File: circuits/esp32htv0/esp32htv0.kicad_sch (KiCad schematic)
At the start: 42 parts, among them J1 Power, J2 UART, SW1 EN, SW2 BOOT, U1 LD1117S33TR_SOT223, U2 ESP32-WROOM-32UE, U3 BME280

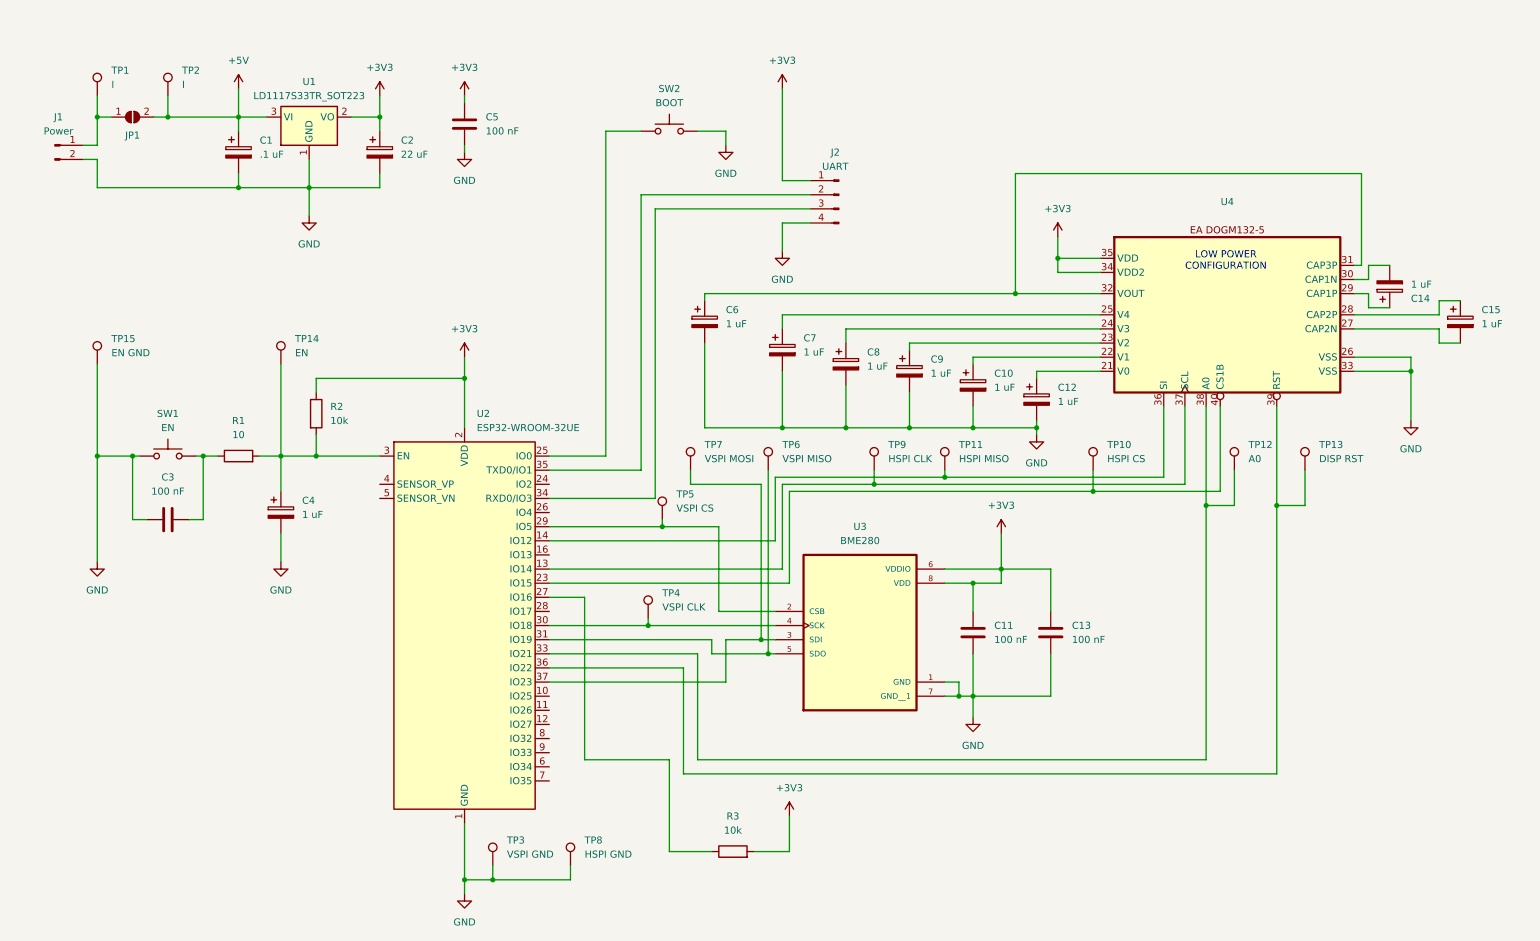
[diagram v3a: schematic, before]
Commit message: Adding data-sheets, documentation and updated circuit for the ESP32 HTV project
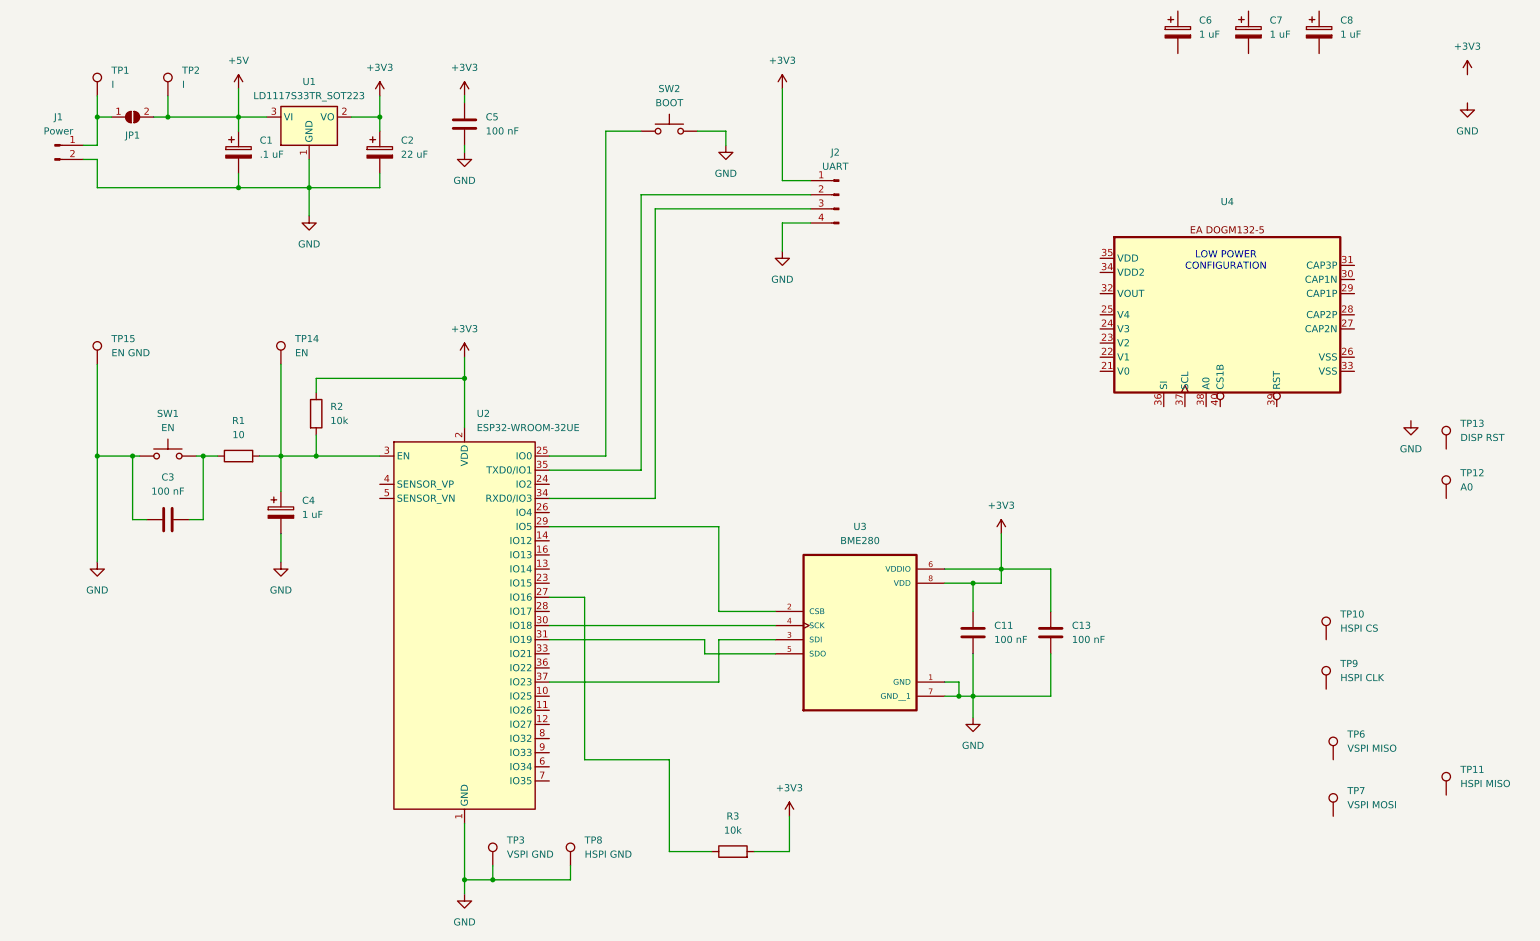
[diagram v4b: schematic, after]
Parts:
- removed C10, C12, C14, C15, C9: 1 uF, Capacitor_SMD:C_1206_3216Metric_Pad1.33x1.80mm_HandSolder, symbol Device:C_Polarized
- removed TP4: VSPI CLK, TestPoint:TestPoint_Loop_D2.50mm_Drill1.0mm, symbol Connector:TestPoint
- removed TP5: VSPI CS, TestPoint:TestPoint_Loop_D2.50mm_Drill1.0mm, symbol Connector:TestPoint
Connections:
- net +3V3: no longer U4.34 (VDD2), U4.35 (VDD)
- net GND: no longer C6.2, C7.2, C8.2, U4.26 (VSS), U4.33 (VSS)
- net at U4.24 (V3): no longer C8.1
- net at U4.25 (V4): no longer C7.1
- net at U2.31 (IO19), U3.5 (SDO): no longer TP6.1
- net at U2.37 (IO23), U3.3 (SDI): no longer TP7.1
- now unconnected: C6.1, TP10.1, TP11.1, TP12.1, TP13.1, TP9.1, U2.13 (IO14), U2.14 (IO12), U2.23 (IO15), U2.33 (IO21), U2.36 (IO22), U4.31 (CAP3P), U4.32 (VOUT), U4.36 (SI), U4.37 (SCL), U4.38 (A0), U4.39 (RST), U4.40 (CS1B)
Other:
- moved on the sheet: C6, C7, C8, TP10, TP11, TP12, TP13, TP6, TP7, TP9

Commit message: Upgrade the ESP32 HTV prototype with DOGS102 display
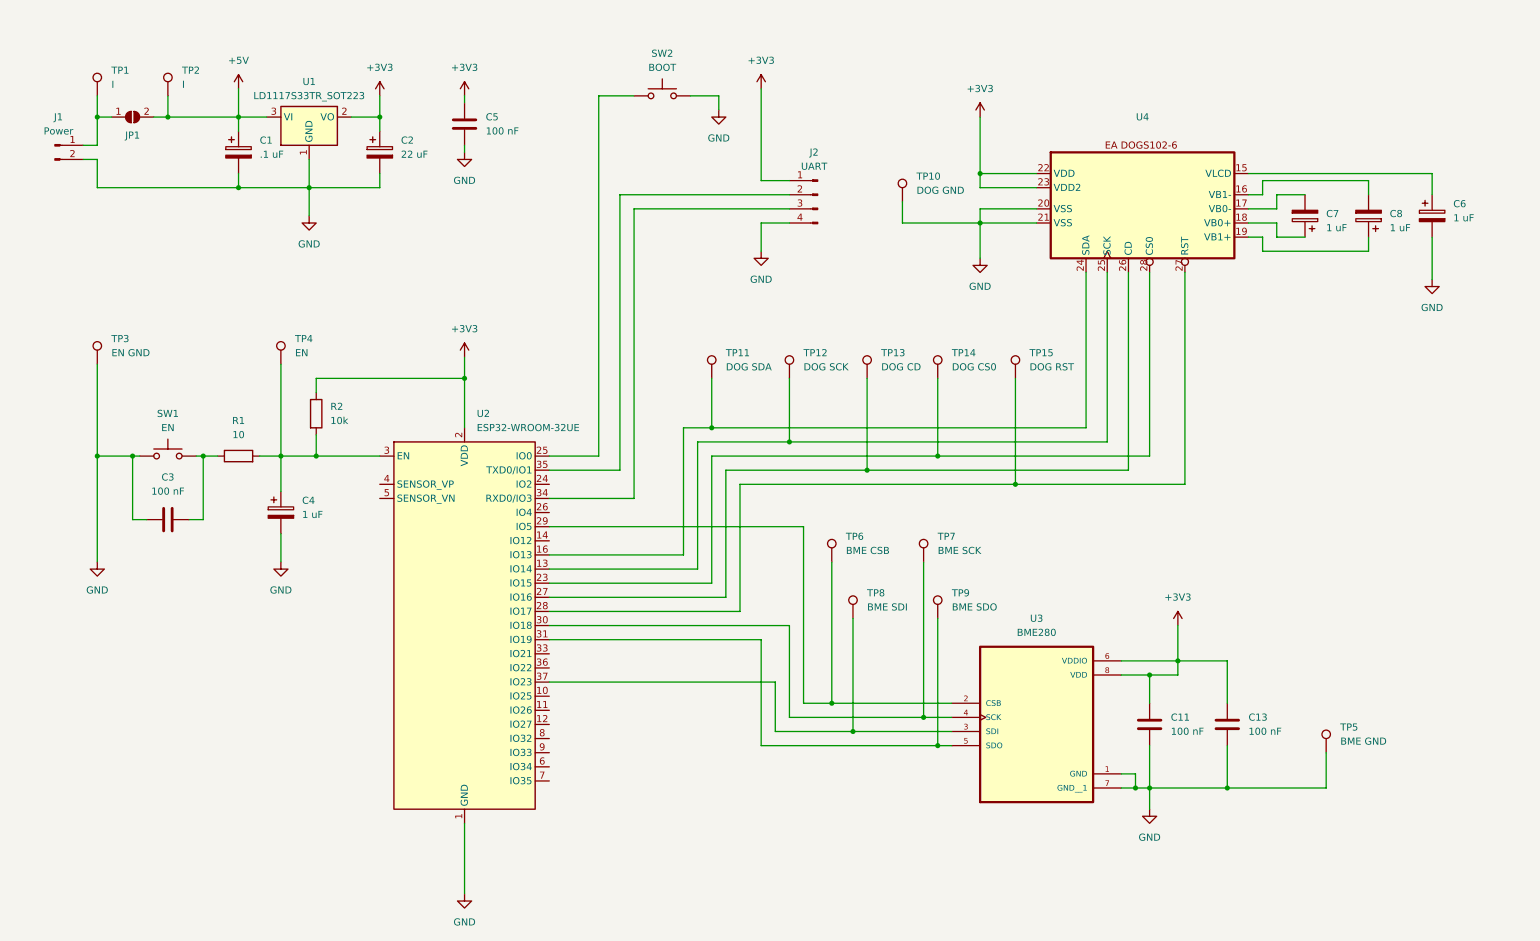
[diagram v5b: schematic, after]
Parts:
- removed R3: 10k, Resistor_SMD:R_1206_3216Metric_Pad1.30x1.75mm_HandSolder, symbol Device:R
- removed U4: ~, gos:DOGM132-5, symbol gos:DOGM132
- added TP14: DOG CS0, TestPoint:TestPoint_Loop_D2.50mm_Drill1.0mm, symbol Connector:TestPoint
- added TP15: DOG RST, TestPoint:TestPoint_Loop_D2.50mm_Drill1.0mm, symbol Connector:TestPoint
- added U4: ~, gos:DOGS102-6, symbol gos:DOGS102
- TP10: value HSPI CS -> DOG GND
- TP11: value HSPI MISO -> DOG SDA
- TP12: value A0 -> DOG SCK
- TP13: value DISP RST -> DOG CD
- TP5: renamed from TP3; value VSPI GND -> BME GND
- TP6: value VSPI MISO -> BME CSB
- TP7: value VSPI MOSI -> BME SCK
- TP8: value HSPI GND -> BME SDI
- TP9: value HSPI CLK -> BME SDO
- renumbered TP15 to TP3, TP14 to TP4
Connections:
- net +3V3: now also U4.22 (VDD), U4.23 (VDD2)
- net GND: now also C6.2, TP10.1, U4.20 (VSS), U4.21 (VSS); no longer TP8.1
- net at TP9.1: now also U2.31 (IO19), U3.5 (SDO)
- net at U2.27 (IO16): now also TP13.1, U4.26 (CD)
- net at U2.13 (IO14): now also TP12.1, U4.25 (SCK)
- net at U2.16 (IO13): now also TP11.1, U4.24 (SDA)
- net at U2.23 (IO15): now also TP14.1, U4.28 (CS0)
- net at U2.28 (IO17): now also TP15.1, U4.27 (RST)
- net at U2.29 (IO5), U3.2 (CSB): now also TP6.1
- net at U2.30 (IO18), U3.4 (SCK): now also TP7.1
- net at U2.37 (IO23), U3.3 (SDI): now also TP8.1
- net at C8.1: now also U4.19 (VB1+)
- net at C8.2: now also U4.16 (VB1-)
- net at C6.1: now also U4.15 (VLCD)
- net at C7.1: now also U4.18 (VB0+)
- net at C7.2: now also U4.17 (VB0-)
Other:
- note removed: "LOW POWER CONFIGURATION"
- moved on the sheet: C11, C13, C6, C7, C8, J2, SW2, TP10, TP11, TP12, TP13, TP5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
